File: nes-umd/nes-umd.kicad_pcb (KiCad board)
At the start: 2 copper layers, 20.3 x 99.1 mm, 2 parts, among them CON101 NES-CONN, CON102 UMD-CONN

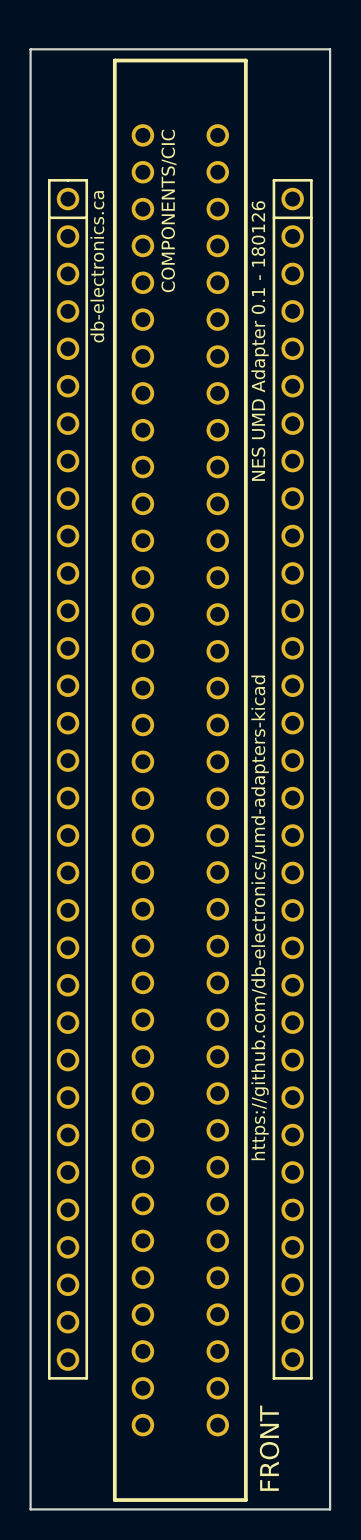
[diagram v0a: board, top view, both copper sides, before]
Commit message: parts placement for ID register
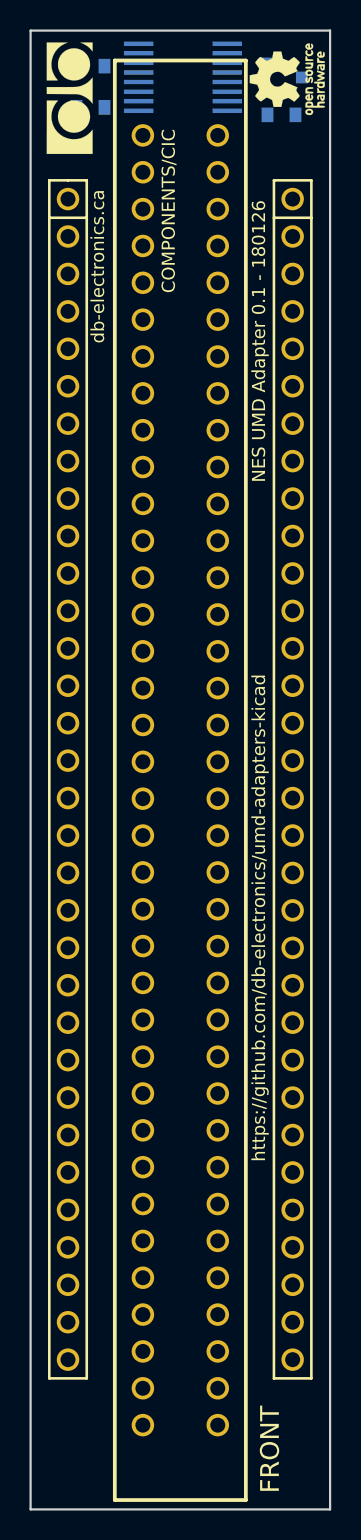
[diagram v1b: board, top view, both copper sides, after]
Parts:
- added C101: 0.1uF/50V, db-smt:0603, B.Cu at (120.9, 63.2)
- added G***: LOGO, db-artwork:db-logo_7.5mm, F.Cu at (119.5, 65.3)
- added G***: LOGO, db-artwork:oshw-logo_5mm, F.Cu at (134.2, 64.1)
- added Q101: SMMBT3904LT1G, db-smt:SOT23, B.Cu at (134.0, 63.9)
- added R101: 10k, db-smt:0603, B.Cu at (120.9, 66.0)
- added R102: 10k, db-smt:0603, B.Cu at (133.8, 66.5)
- added U101: MC74HC589ADTR2G, db-smt:TSSOP-16, B.Cu at (130.1, 61.6)
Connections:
- CON101 pad 1: (no net) -> GND
- CON101 pad 10: (no net) -> /A3
- CON101 pad 11: (no net) -> /A2
- CON101 pad 12: (no net) -> /A1
- CON101 pad 13: (no net) -> /A0
- CON101 pad 14: (no net) -> /~PWR
- CON101 pad 2: (no net) -> /A11
- CON101 pad 23: (no net) -> /A6
- CON101 pad 24: (no net) -> /A5
- CON101 pad 26: (no net) -> /A3
- CON101 pad 27: (no net) -> /A2
- CON101 pad 28: (no net) -> /A1
- CON101 pad 29: (no net) -> /A0
- CON101 pad 3: (no net) -> /A10
- CON101 pad 30: (no net) -> /D0
- CON101 pad 31: (no net) -> /D1
- CON101 pad 32: (no net) -> /D2
- CON101 pad 33: (no net) -> /D3
- CON101 pad 36: (no net) -> +5V
- CON101 pad 39: (no net) -> /A12
- CON101 pad 4: (no net) -> /A9
- CON101 pad 40: (no net) -> /A13
- CON101 pad 41: (no net) -> /A14
- CON101 pad 42: (no net) -> /D7
- CON101 pad 43: (no net) -> /D6
- CON101 pad 44: (no net) -> /D5
- CON101 pad 45: (no net) -> /D4
- CON101 pad 46: (no net) -> /D3
- CON101 pad 47: (no net) -> /D2
- CON101 pad 48: (no net) -> /D1
- CON101 pad 49: (no net) -> /D0
- CON101 pad 5: (no net) -> /A8
- CON101 pad 50: (no net) -> /~PCE
- CON101 pad 59: (no net) -> /A7
- CON101 pad 6: (no net) -> /A7
- CON101 pad 60: (no net) -> /A8
- CON101 pad 61: (no net) -> /A9
- CON101 pad 62: (no net) -> /A11
- CON101 pad 63: (no net) -> /A10
- CON101 pad 64: (no net) -> /A12
- CON101 pad 66: (no net) -> /D7
- CON101 pad 67: (no net) -> /D6
- CON101 pad 68: (no net) -> /D5
- CON101 pad 69: (no net) -> /D4
- CON101 pad 7: (no net) -> /A6
- CON101 pad 72: (no net) -> GND
- CON101 pad 8: (no net) -> /A5
- CON101 pad 9: (no net) -> /A4
- CON102 pad 10: (no net) -> +5V
- CON102 pad 14: (no net) -> /A14
- CON102 pad 15: (no net) -> /A13
- CON102 pad 18: (no net) -> /A12
- CON102 pad 19: (no net) -> /A7
- CON102 pad 20: (no net) -> /D7
- CON102 pad 21: (no net) -> /D6
- CON102 pad 22: (no net) -> /A6
- CON102 pad 23: (no net) -> /A5
- CON102 pad 24: (no net) -> /D5
- CON102 pad 25: (no net) -> /D4
- CON102 pad 26: (no net) -> /A4
- CON102 pad 31: (no net) -> +5V
- CON102 pad 32: (no net) -> GND
- CON102 pad 33: (no net) -> GND
- CON102 pad 34: (no net) -> +5V
- CON102 pad 39: (no net) -> /A3
- CON102 pad 40: (no net) -> /D3
- CON102 pad 41: (no net) -> /D2
- CON102 pad 42: (no net) -> /A2
- CON102 pad 43: (no net) -> /A1
- CON102 pad 44: (no net) -> /D1
- CON102 pad 45: (no net) -> /D0
- CON102 pad 46: (no net) -> /A0
- CON102 pad 47: (no net) -> /A11
- CON102 pad 50: (no net) -> /A10
- CON102 pad 51: (no net) -> /A9
- CON102 pad 54: (no net) -> /A8
- CON102 pad 55: (no net) -> GND
- CON102 pad 56: (no net) -> /~ID
- CON102 pad 57: (no net) -> /~PWR
- CON102 pad 58: (no net) -> /~RST
- CON102 pad 62: (no net) -> /SCK
- CON102 pad 63: (no net) -> /MISO
- CON102 pad 9: (no net) -> /~PCE
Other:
- board size 20.3 x 99.1 mm -> 20.3 x 100.3 mm
